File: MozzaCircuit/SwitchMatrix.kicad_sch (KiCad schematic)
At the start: 94 parts, among them SW13 SW_ChocV2_rev, SW14 SW_ChocV2_rev, SW15 SW_ChocV2_rev, SW21 SW_ChocV2_rev, SW22 SW_ChocV2_rev, SW23 SW_ChocV2_rev, SW24 SW_ChocV2_rev, SW25 SW_ChocV2_rev, SW31 SW_ChocV2_rev, SW32 SW_ChocV2_rev, SW33 SW_ChocV2_rev, SW34 SW_ChocV2_rev, SW35 SW_ChocV2_rev, SW41 SW_ChocV2_rev, SW42 SW_ChocV2_rev, SW43 SW_ChocV2_rev, SW44 SW_ChocV2_rev, SW51 SW_ChocV2_rev, SW52 SW_ChocV2_rev, SW53 SW_ChocV2_rev, SW54 SW_ChocV2_rev, SW61 SW_ChocV2_rev, SW62 SW_ChocV2_rev, SW63 SW_ChocV2_rev, SW64 SW_ChocV2_rev, SW71 SW_ChocV2_rev, SW72 SW_ChocV2_rev, SW73 SW_ChocV2_rev, SW82 SW_ChocV2_rev, SW83 SW_ChocV2_rev, SW84 SW_ChocV2_rev

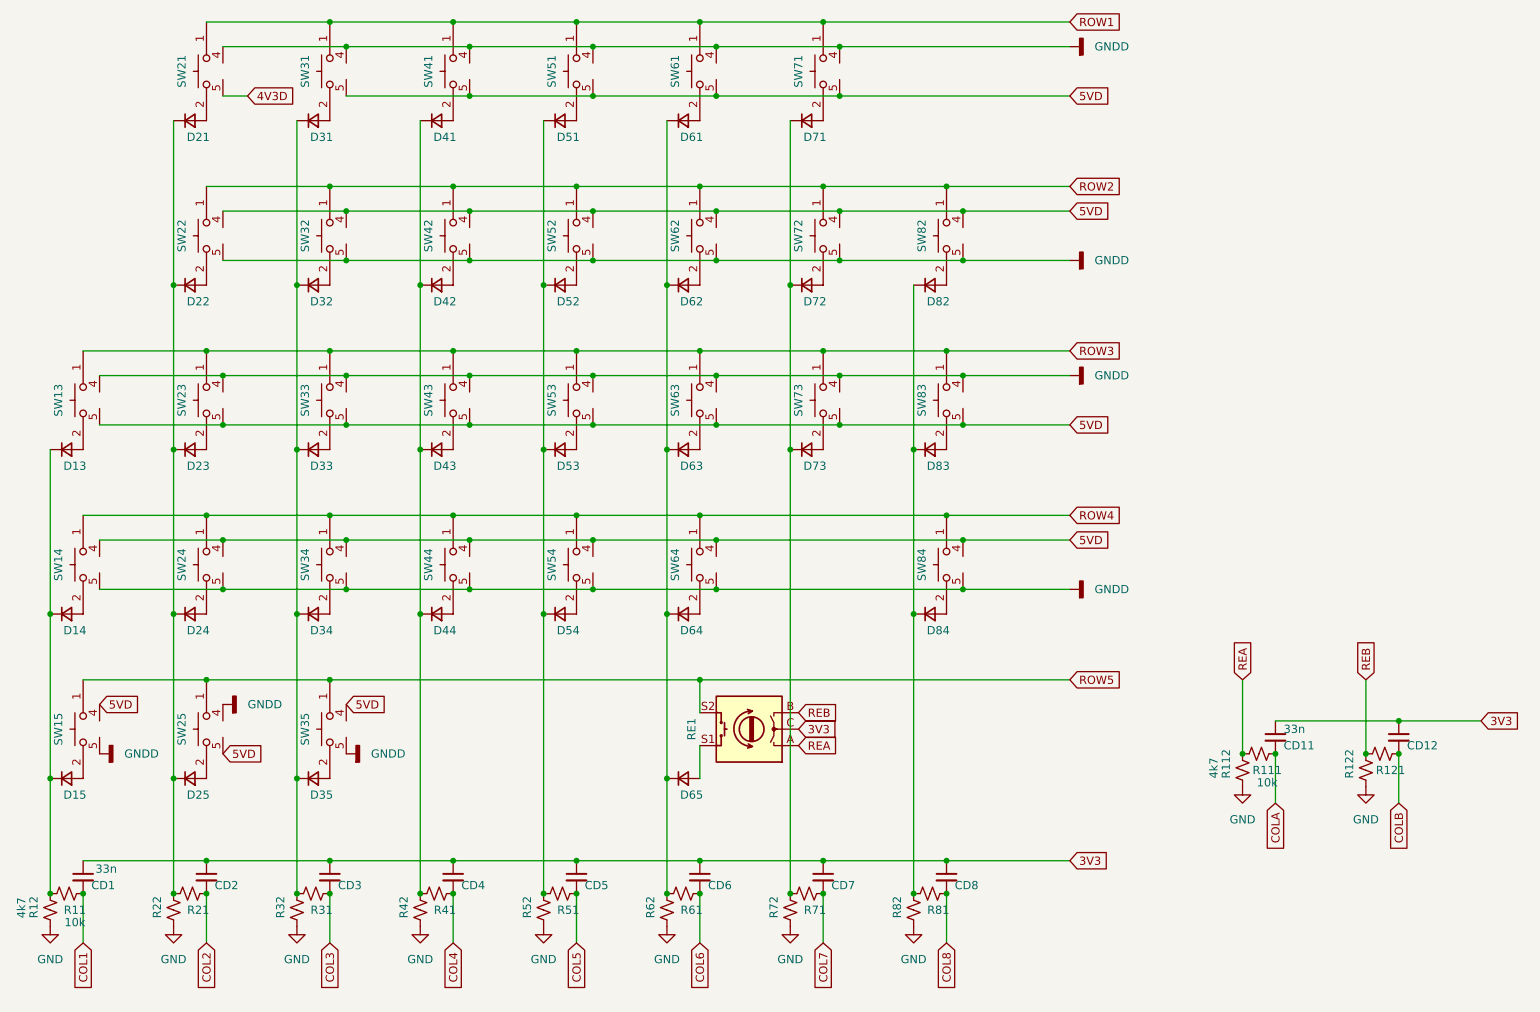
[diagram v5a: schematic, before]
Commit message: changed row lines to have better ground fill
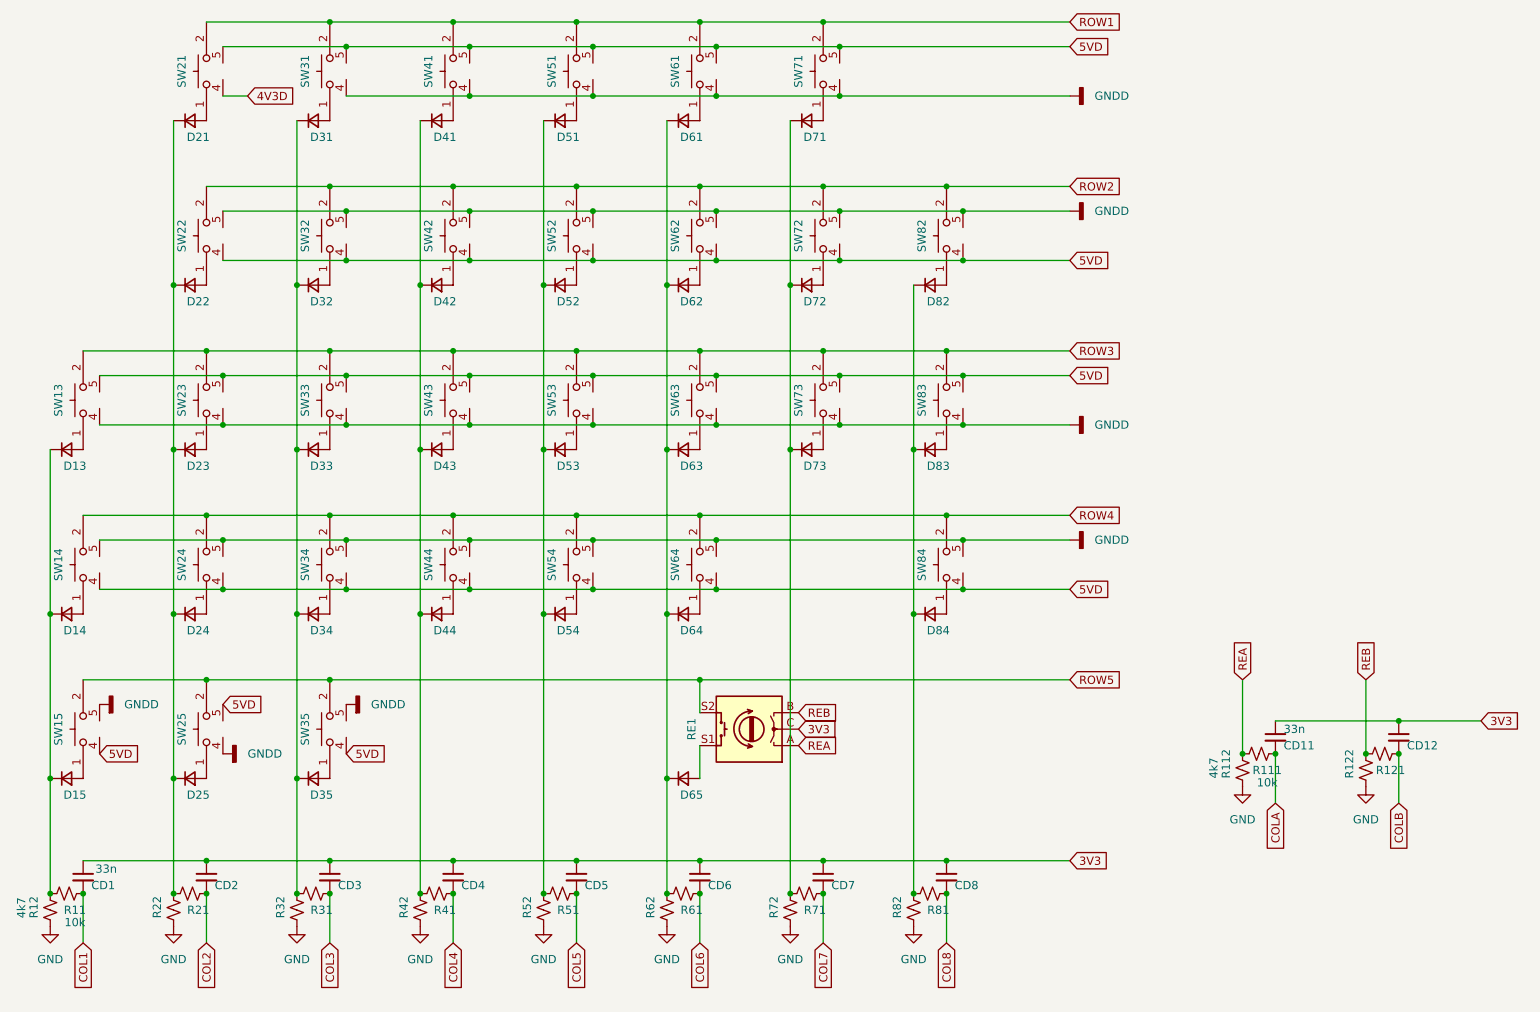
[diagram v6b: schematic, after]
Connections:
- net 4V3D: now also SW21.4; no longer SW21.5
- net 5VD: now also SW21.5
- net GNDD: no longer SW21.4
- net ROW1: now also SW21.2, SW21.3, SW31.2, SW31.3, SW41.2, SW41.3, SW51.2, SW51.3, SW61.2, SW61.3, SW71.2, SW71.3; no longer SW21.1, SW31.1, SW41.1, SW51.1, SW61.1, SW71.1
- net ROW2: now also SW22.2, SW22.3, SW32.2, SW32.3, SW42.2, SW42.3, SW52.2, SW52.3, SW62.2, SW62.3, SW72.2, SW72.3, SW82.2, SW82.3; no longer SW22.1, SW32.1, SW42.1, SW52.1, SW62.1, SW72.1, SW82.1
- net ROW3: now also SW13.2, SW13.3, SW23.2, SW23.3, SW33.2, SW33.3, SW43.2, SW43.3, SW53.2, SW53.3, SW63.2, SW63.3, SW73.2, SW73.3, SW83.2, SW83.3; no longer SW13.1, SW23.1, SW33.1, SW43.1, SW53.1, SW63.1, SW73.1, SW83.1
- net ROW4: now also SW14.2, SW14.3, SW24.2, SW24.3, SW34.2, SW34.3, SW44.2, SW44.3, SW54.2, SW54.3, SW64.2, SW64.3, SW84.2, SW84.3; no longer SW14.1, SW24.1, SW34.1, SW44.1, SW54.1, SW64.1, SW84.1
- net ROW5: now also SW15.2, SW15.3, SW25.2, SW25.3, SW35.2, SW35.3; no longer SW15.1, SW25.1, SW35.1
- new net: D23.2 (A), SW23.1
- new net: D54.2 (A), SW54.1
- new net: D22.2 (A), SW22.1
- new net: D44.2 (A), SW44.1
- new net: D34.2 (A), SW34.1
- new net: D35.2 (A), SW35.1
- new net: D21.2 (A), SW21.1
- new net: D15.2 (A), SW15.1
- new net: D42.2 (A), SW42.1
- new net: D24.2 (A), SW24.1
- new net: D13.2 (A), SW13.1
- new net: D32.2 (A), SW32.1
- new net: D72.2 (A), SW72.1
- new net: D53.2 (A), SW53.1
- new net: D73.2 (A), SW73.1
- new net: D41.2 (A), SW41.1
- new net: D43.2 (A), SW43.1
- new net: D83.2 (A), SW83.1
- new net: D52.2 (A), SW52.1
- new net: D14.2 (A), SW14.1
- new net: D62.2 (A), SW62.1
- new net: D63.2 (A), SW63.1
- new net: D71.2 (A), SW71.1
- new net: D33.2 (A), SW33.1
- new net: D51.2 (A), SW51.1
- new net: D61.2 (A), SW61.1
- new net: D25.2 (A), SW25.1
- new net: D84.2 (A), SW84.1
- new net: D64.2 (A), SW64.1
- new net: D31.2 (A), SW31.1
- new net: D82.2 (A), SW82.1

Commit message: fixed drc errors
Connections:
- net 4V3D: now also SW21.5; no longer SW21.4
- net 5VD: no longer SW21.5
- net GNDD: now also SW21.4
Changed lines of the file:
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@@
   (junction (at 72.39 113.03) (diameter 0) (color 0 0 0 0)
   )
+  (junction (at 72.39 36.83) (diameter 0) (color 0 0 0 0)
+  )
   (junction (at 69.85 76.2) (diameter 0) (color 0 0 0 0)
   )
@@
   (junction (at 69.85 154.94) (diameter 0) (color 0 0 0 0)
   )
-  (junction (at 72.39 29.21) (diameter 0) (color 0 0 0 0)
-  )
   (junction (at 140.97 66.04) (diameter 0) (color 0 0 0 0)
   )
@@
     (stroke (width 0) (type default) (color 0 0 0 0))
   )
-  (wire (pts (xy 53.34 36.83) (xy 57.15 36.83))
-    (stroke (width 0) (type default) (color 0 0 0 0))
-  )
   (wire (pts (xy 72.39 29.21) (xy 91.44 29.21))
     (stroke (width 0) (type default) (color 0 0 0 0))
@@
     (stroke (width 0) (type default) (color 0 0 0 0))
   )
+  (wire (pts (xy 53.34 36.83) (xy 72.39 36.83))
+    (stroke (width 0) (type default) (color 0 0 0 0))
+  )
   (wire (pts (xy 31.75 76.2) (xy 50.8 76.2))
     (stroke (width 0) (type default) (color 0 0 0 0))
@@
   )
   (wire (pts (xy 160.02 91.44) (xy 160.02 116.84))
-    (stroke (width 0) (type default) (color 0 0 0 0))
-  )
-  (wire (pts (xy 53.34 29.21) (xy 72.39 29.21))
     (stroke (width 0) (type default) (color 0 0 0 0))
   )
@@
     )
   )
-  (global_label "4V3D" (shape input) (at 57.15 36.83 0) (fields_autoplaced)
-    (effects (font (size 1.27 1.27)) (justify left))
-    (property "Intersheet References" "${INTERSHEET_REFS}" (id 0) (at 64.3407 36.7506 0)
-      (effects (font (size 1.27 1.27)) (justify left) hide)
-    )
+  (global_label "4V3D" (shape input) (at 53.34 29.21 0) (fields_autoplaced)
+    (effects (font (size 1.27 1.27)) (justify left))
+    (property "Intersheet References" "${INTERSHEET_REFS}" (id 0) (at 60.5307 29.1306 0)
+      (effects (font (size 1.27 1.27)) (justify left) hide)
+    )

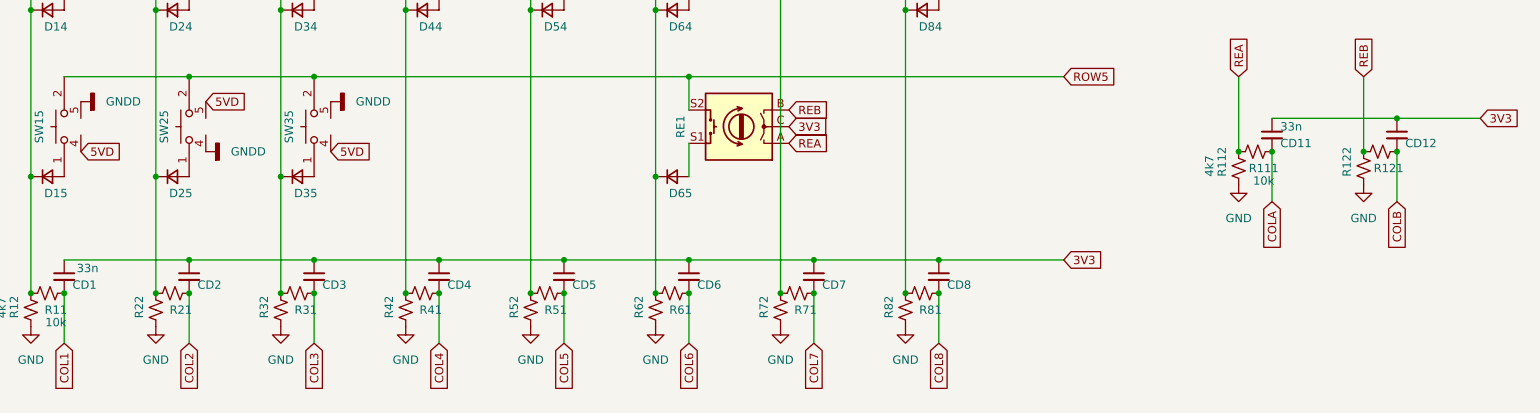
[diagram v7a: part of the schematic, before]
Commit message: cap/resister values
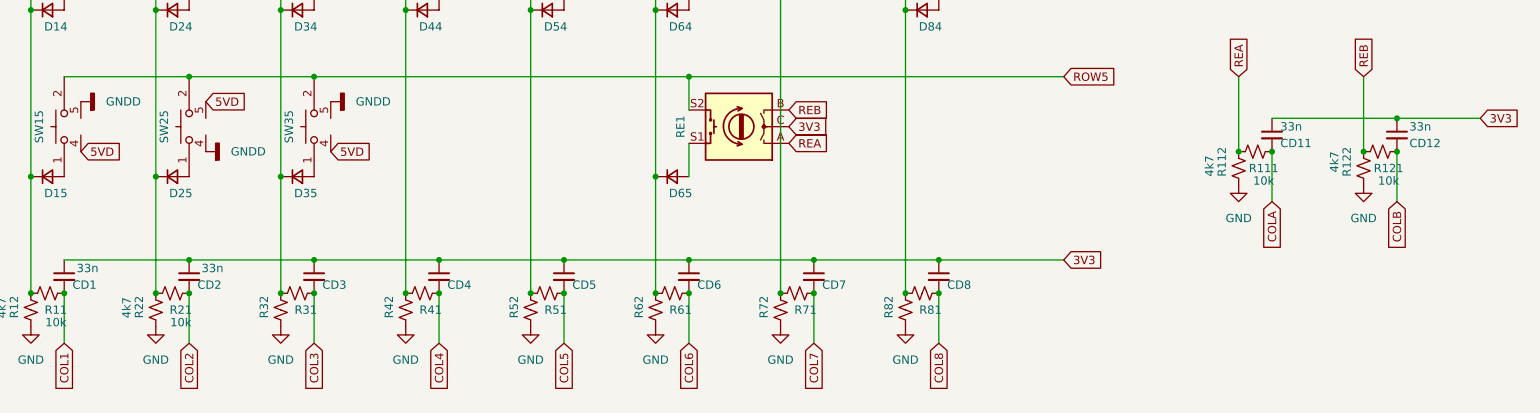
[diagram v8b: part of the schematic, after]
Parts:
- CD12, CD2, CD3, CD4, CD5, CD6, CD7, CD8: value C_Small -> 33n
- R121, R21, R31, R41, R51, R61, R71, R81: value R_Small_US -> 10k
- R122, R22, R32, R42, R52, R62, R72, R82: value R_Small_US -> 4k7
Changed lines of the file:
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@@
       (effects (font (size 1.27 1.27)) (justify left))
     )
-    (property "Value" "C_Small" (id 1) (at 129.54 158.7562 0)
+    (property "Value" "33n" (id 1) (at 129.54 158.7562 0)
       (effects (font (size 1.27 1.27)) (justify left) hide)
     )
@@
       (effects (font (size 1.27 1.27)) (justify left))
     )
-    (property "Value" "R_Small_US" (id 1) (at 48.26 163.8299 0)
-      (effects (font (size 1.27 1.27)) (justify left) hide)
+    (property "Value" "4k7" (id 1) (at 41.275 163.83 90)
+      (effects (font (size 1.27 1.27)) (justify left))
     )
     (property "Footprint" "00_KeyParts:R_1608_HandSolder_both_sides" (id 2) (at 45.72 162.56 0)
@@
     (in_bom yes) (on_board yes)
     (property "Reference" "R81" (id 0) (at 163.83 162.56 90))
-    (property "Value" "R_Small_US" (id 1) (at 162.56 156.21 90)
+    (property "Value" "10k" (id 1) (at 162.56 156.21 90)
       (effects (font (size 1.27 1.27)) hide)
     )
@@
       (effects (font (size 1.27 1.27)) (justify left))
     )
-    (property "Value" "C_Small" (id 1) (at 148.59 158.7562 0)
+    (property "Value" "33n" (id 1) (at 148.59 158.7562 0)
       (effects (font (size 1.27 1.27)) (justify left) hide)
     )
@@
     (in_bom yes) (on_board yes)
     (property "Reference" "R61" (id 0) (at 125.73 162.56 90))
-    (property "Value" "R_Small_US" (id 1) (at 124.46 156.21 90)
+    (property "Value" "10k" (id 1) (at 124.46 156.21 90)
       (effects (font (size 1.27 1.27)) hide)
     )
@@
       (effects (font (size 1.27 1.27)) (justify left))
     )
-    (property "Value" "R_Small_US" (id 1) (at 105.41 163.8299 0)
+    (property "Value" "4k7" (id 1) (at 105.41 163.8299 0)
       (effects (font (size 1.27 1.27)) (justify left) hide)
     )
@@
       (effects (font (size 1.27 1.27)) (justify left))
     )
-    (property "Value" "R_Small_US" (id 1) (at 162.56 163.8299 0)
+    (property "Value" "4k7" (id 1) (at 162.56 163.8299 0)
       (effects (font (size 1.27 1.27)) (justify left) hide)
     )
@@
       (effects (font (size 1.27 1.27)) (justify left))
     )
-    (property "Value" "C_Small" (id 1) (at 53.34 158.7562 0)
-      (effects (font (size 1.27 1.27)) (justify left) hide)
+    (property "Value" "33n" (id 1) (at 52.705 156.21 0)
+      (effects (font (size 1.27 1.27)) (justify left))
     )
     (property "Footprint" "00_KeyParts:C_1608_HandSolder_both_sides" (id 2) (at 50.8 157.48 0)
@@
     (in_bom yes) (on_board yes)
     (property "Reference" "R121" (id 0) (at 233.68 140.97 90))
-    (property "Value" "R_Small_US" (id 1) (at 232.41 134.62 90)
-      (effects (font (size 1.27 1.27)) hide)
-    )
+    (property "Value" "10k" (id 1) (at 233.68 142.875 90))
     (property "Footprint" "00_KeyParts:R_1608_HandSolder_both_sides" (id 2) (at 232.41 138.43 0)
       (effects (font (size 1.27 1.27)) hide)
@@
       (effects (font (size 1.27 1.27)) (justify left))
     )
-    (property "Value" "C_Small" (id 1) (at 110.49 158.7562 0)
+    (property "Value" "33n" (id 1) (at 110.49 158.7562 0)
       (effects (font (size 1.27 1.27)) (justify left) hide)
     )
@@
       (effects (font (size 1.27 1.27)) (justify left))
     )
-    (property "Value" "C_Small" (id 1) (at 72.39 158.7562 0)
+    (property "Value" "33n" (id 1) (at 72.39 158.7562 0)
       (effects (font (size 1.27 1.27)) (justify left) hide)
     )
@@
       (effects (font (size 1.27 1.27)) (justify left))
     )
-    (property "Value" "R_Small_US" (id 1) (at 124.46 163.8299 0)
+    (property "Value" "4k7" (id 1) (at 124.46 163.8299 0)
       (effects (font (size 1.27 1.27)) (justify left) hide)
     )
@@
       (effects (font (size 1.27 1.27)) (justify left))
     )
-    (property "Value" "C_Small" (id 1) (at 91.44 158.7562 0)
+    (property "Value" "33n" (id 1) (at 91.44 158.7562 0)
       (effects (font (size 1.27 1.27)) (justify left) hide)
     )
@@
       (effects (font (size 1.27 1.27)) (justify left))
     )
-    (property "Value" "C_Small" (id 1) (at 167.64 158.7562 0)
+    (property "Value" "33n" (id 1) (at 167.64 158.7562 0)
       (effects (font (size 1.27 1.27)) (justify left) hide)
     )
@@
       (effects (font (size 1.27 1.27)) (justify left))
     )
-    (property "Value" "R_Small_US" (id 1) (at 86.36 163.8299 0)
+    (property "Value" "4k7" (id 1) (at 86.36 163.8299 0)
       (effects (font (size 1.27 1.27)) (justify left) hide)
     )
@@
   (symbol (lib_id "Device:C_Small") (at 234.95 135.89 0) (unit 1)
     (in_bom yes) (on_board yes)
-    (property "Reference" "CD12" (id 0) (at 236.22 137.16 0)
-      (effects (font (size 1.27 1.27)) (justify left))
-    )
-    (property "Value" "C_Small" (id 1) (at 237.49 137.1662 0)
-      (effects (font (size 1.27 1.27)) (justify left) hide)
+    (property "Reference" "CD12" (id 0) (at 236.855 137.16 0)
+      (effects (font (size 1.27 1.27)) (justify left))
+    )
+    (property "Value" "33n" (id 1) (at 236.855 134.62 0)
+      (effects (font (size 1.27 1.27)) (justify left))
     )
     (property "Footprint" "00_KeyParts:C_1608_HandSolder_both_sides" (id 2) (at 234.95 135.89 0)
@@
     (in_bom yes) (on_board yes)
     (property "Reference" "R51" (id 0) (at 106.68 162.56 90))
-    (property "Value" "R_Small_US" (id 1) (at 105.41 156.21 90)
+    (property "Value" "10k" (id 1) (at 105.41 156.21 90)
       (effects (font (size 1.27 1.27)) hide)
     )
@@
       (effects (font (size 1.27 1.27)) (justify left))
     )
-    (property "Value" "R_Small_US" (id 1) (at 67.31 163.8299 0)
+    (property "Value" "4k7" (id 1) (at 67.31 163.8299 0)
       (effects (font (size 1.27 1.27)) (justify left) hide)
     )
@@
       (effects (font (size 1.27 1.27)) (justify left))
     )
-    (property "Value" "R_Small_US" (id 1) (at 232.41 142.2399 0)
-      (effects (font (size 1.27 1.27)) (justify left) hide)
+    (property "Value" "4k7" (id 1) (at 225.425 141.605 90)
+      (effects (font (size 1.27 1.27)) (justify left))
     )
     (property "Footprint" "00_KeyParts:R_1608_HandSolder_both_sides" (id 2) (at 229.87 140.97 0)
@@
     (in_bom yes) (on_board yes)
     (property "Reference" "R41" (id 0) (at 87.63 162.56 90))
-    (property "Value" "R_Small_US" (id 1) (at 86.36 156.21 90)
+    (property "Value" "10k" (id 1) (at 86.36 156.21 90)
       (effects (font (size 1.27 1.27)) hide)
     )
@@
     (in_bom yes) (on_board yes)
     (property "Reference" "R31" (id 0) (at 68.58 162.56 90))
-    (property "Value" "R_Small_US" (id 1) (at 67.31 156.21 90)
+    (property "Value" "10k" (id 1) (at 67.31 156.21 90)
       (effects (font (size 1.27 1.27)) hide)
     )
@@
       (effects (font (size 1.27 1.27)) (justify left))
     )
-    (property "Value" "R_Small_US" (id 1) (at 143.51 163.8299 0)
+    (property "Value" "4k7" (id 1) (at 143.51 163.8299 0)
       (effects (font (size 1.27 1.27)) (justify left) hide)
     )
@@
     (in_bom yes) (on_board yes)
     (property "Reference" "R21" (id 0) (at 49.53 162.56 90))
-    (property "Value" "R_Small_US" (id 1) (at 48.26 156.21 90)
-      (effects (font (size 1.27 1.27)) hide)
-    )
+    (property "Value" "10k" (id 1) (at 49.53 164.465 90))
     (property "Footprint" "00_KeyParts:R_1608_HandSolder_both_sides" (id 2) (at 48.26 160.02 0)
       (effects (font (size 1.27 1.27)) hide)
@@
     (in_bom yes) (on_board yes)
     (property "Reference" "R71" (id 0) (at 144.78 162.56 90))
-    (property "Value" "R_Small_US" (id 1) (at 143.51 156.21 90)
-      (effects (font (size 1.27 1.27)) hide)
-    )
+    (property "Value" "10k" (id 1) (at 143.51 156.21 90)
+      (effects (font (size 1.27 1.27)) hide)
+    )
